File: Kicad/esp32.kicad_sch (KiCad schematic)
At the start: 29 parts, among them J3 TC2030-IDC, J4 Conn_01x04, J5 USB_C_Receptacle_USB2.0, SW1 GT-TC029B-H025-L1N, SW2 GT-TC029B-H025-L1N, U6 RT9080-33GJ5, U7 ESP32-S3-WROOM-1, Y1 32.768kHz

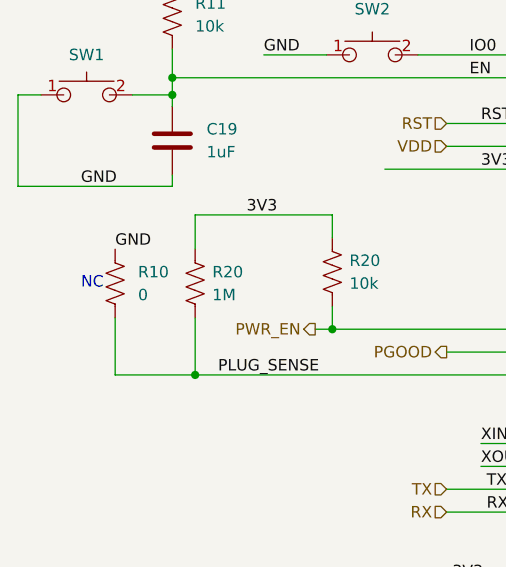
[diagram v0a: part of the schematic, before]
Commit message: Updating Bill Of Materials
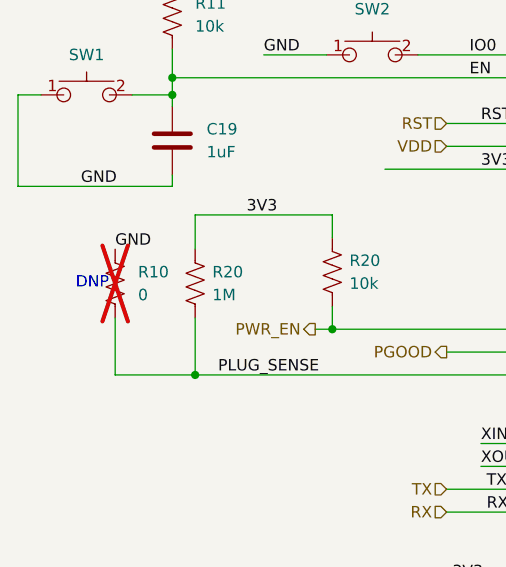
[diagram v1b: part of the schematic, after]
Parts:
- R10: now not fitted
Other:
- note added: "DNP"
- note removed: "NC"
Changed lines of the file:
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@@
 		)
 	)
-	(text "NC"
+	(text "DNP"
 		(exclude_from_sim no)
 		(at 26.67 102.87 0)
@@
 		(in_bom yes)
 		(on_board yes)
-		(dnp no)
+		(dnp yes)
 		(fields_autoplaced yes)
 		(property "Reference" "R10"

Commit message: V0.35 Release
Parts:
- removed R10: 0, Resistor_SMD:R_0402_1005Metric, symbol Device:R_US
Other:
- note removed: "DNP"
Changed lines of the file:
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@@
-	)
-	(junction
-		(at 38.1 113.03)
-		(diameter 0)
-		(color 0 0 0 0)
 	)
 	(junction
@@
 	(wire
 		(pts
-			(xy 29.21 113.03) (xy 29.21 106.68)
-		)
-		(stroke
-			(width 0)
-			(type default)
-		)
-	)
-	(wire
-		(pts
 			(xy 40.005 29.21) (xy 42.545 29.21)
 		)
@@
 		(pts
 			(xy 191.77 80.01) (xy 214.63 80.01)
-		)
-		(stroke
-			(width 0)
-			(type default)
-		)
-	)
-	(wire
-		(pts
-			(xy 38.1 113.03) (xy 29.21 113.03)
 		)
 		(stroke
@@
 		)
 	)
-	(text "DNP"
-		(exclude_from_sim no)
-		(at 26.67 102.87 0)
-		(effects
-			(font
-				(size 1.27 1.27)
-			)
-		)
-	)
 	(text "ESP32 3V3 LDO"
 		(exclude_from_sim no)
@@
 	(label "P_RX"
 		(at 51.435 170.815 0)
-		(fields_autoplaced yes)
-		(effects
-			(font
-				(size 1.27 1.27)
-			)
-			(justify left bottom)
-		)
-	)
-	(label "GND"
-		(at 29.21 99.06 0)
-		(fields_autoplaced yes)
 		(effects
 			(font
@@
 	(label "RST"
 		(at 69.85 85.09 0)
-		(fields_autoplaced yes)
 		(effects
 			(font
@@
 	(label "5V"
 		(at 204.47 53.975 0)
-		(fields_autoplaced yes)
 		(effects
 			(font
@@
 	(label "P_TX"
 		(at 51.435 168.275 0)
-		(fields_autoplaced yes)
 		(effects
 			(font
@@
 	(label "3V3"
 		(at 43.815 95.25 0)
-		(fields_autoplaced yes)
 		(effects
 			(font
@@
 	(label "EN"
 		(at 51.435 165.735 0)
-		(fields_autoplaced yes)
 		(effects
 			(font
@@
 	(label "GND"
 		(at 184.912 29.845 0)
-		(fields_autoplaced yes)
 		(effects
 			(font
@@
 	(label "GND"
 		(at 224.79 92.075 0)
-		(fields_autoplaced yes)
 		(effects
 			(font
@@
 	(label "XOUT32"
 		(at 150.495 29.845 0)
-		(fields_autoplaced yes)
 		(effects
 			(font
@@
 	(label "EN"
 		(at 68.58 80.01 0)
-		(fields_autoplaced yes)
 		(effects
 			(font
@@
 	(label "P_RX"
 		(at 195.58 90.17 0)
-		(fields_autoplaced yes)
 		(effects
 			(font
@@
 	(label "IO0"
 		(at 68.58 77.47 0)
-		(fields_autoplaced yes)
 		(effects
 			(font
@@
 	(label "GND"
 		(at 125.73 68.58 0)
-		(fields_autoplaced yes)
 		(effects
 			(font
@@
 	(label "3V3"
 		(at 66.675 135.89 0)
-		(fields_autoplaced yes)
 		(effects
 			(font
@@
 	(label "SDA"
 		(at 195.58 102.87 0)
-		(fields_autoplaced yes)
 		(effects
 			(font
@@
 	(label "GND"
 		(at 224.79 111.76 90)
-		(fields_autoplaced yes)
 		(effects
 			(font
@@
 	(label "GND"
 		(at 188.595 61.595 0)
-		(fields_autoplaced yes)
 		(effects
 			(font
@@
 	(label "XIN32"
 		(at 69.85 120.65 0)
-		(fields_autoplaced yes)
 		(effects
 			(font
@@
 	(label "TX"
 		(at 70.485 125.73 0)
-		(fields_autoplaced yes)
 		(effects
 			(font
@@
 	(label "GND"
 		(at 138.43 42.545 0)
-		(fields_autoplaced yes)
 		(effects
 			(font
@@
 	(label "3V3"
 		(at 76.835 165.735 0)
-		(fields_autoplaced yes)
 		(effects
 			(font
@@
 	(label "3V3"
 		(at 69.85 90.17 0)
-		(fields_autoplaced yes)
 		(effects
 			(font
@@
 	(label "IO0"
 		(at 76.835 170.815 0)
-		(fields_autoplaced yes)
 		(effects
 			(font
@@
 	(label "SCL"
 		(at 195.58 100.33 0)
-		(fields_autoplaced yes)
 		(effects
 			(font
@@
 	(label "XOUT32"
 		(at 69.85 123.19 0)
-		(fields_autoplaced yes)
 		(effects
 			(font
@@
 	(label "SCL"
 		(at 184.912 34.925 0)
-		(fields_autoplaced yes)
 		(effects
 			(font
@@
 	(label "XIN32"
 		(at 116.84 29.845 0)
-		(fields_autoplaced yes)
 		(effects
 			(font
@@
 	(label "GND"
 		(at 201.93 135.89 0)
-		(fields_autoplaced yes)
 		(effects
 			(font
@@
 	(label "GND"
 		(at 45.72 77.47 0)
-		(fields_autoplaced yes)
 		(effects
 			(font
@@
 	(label "SDA"
 		(at 184.912 37.465 0)
-		(fields_autoplaced yes)
 		(effects
 			(font
@@
 	(label "PLUG_SENSE"
 		(at 40.64 113.03 0)
-		(fields_autoplaced yes)
 		(effects
 			(font
@@
 	(label "3V3"
 		(at 125.73 55.88 0)
-		(fields_autoplaced yes)
 		(effects
 			(font
@@
 	(label "P_TX"
 		(at 195.58 87.63 0)
-		(fields_autoplaced yes)
 		(effects
 			(font
@@
 	(label "3V3"
 		(at 184.912 32.385 0)
-		(fields_autoplaced yes)
 		(effects
 			(font
@@
 	(label "GND"
 		(at 25.4 92.075 0)
-		(fields_autoplaced yes)
 		(effects
 			(font
@@
 	(label "5V"
 		(at 33.655 29.21 0)
-		(fields_autoplaced yes)
 		(effects
 			(font
@@
 	(label "GND"
 		(at 76.835 168.275 0)
-		(fields_autoplaced yes)
 		(effects
 			(font
@@
 	(label "GND"
 		(at 48.895 42.545 0)
-		(fields_autoplaced yes)
 		(effects
 			(font
@@
 	(label "3V3"
 		(at 35.56 66.675 0)
-		(fields_autoplaced yes)
 		(effects
 			(font
@@
 	(label "RX"
 		(at 70.485 128.27 0)
-		(fields_autoplaced yes)
 		(effects
 			(font
@@
 		(shape input)
 		(at 66.04 125.73 180)
-		(fields_autoplaced yes)
 		(effects
 			(font
@@
 		(shape input)
 		(at 66.04 128.27 180)
-		(fields_autoplaced yes)
 		(effects
 			(font
@@
 		(shape input)
 		(at 73.025 29.21 0)
-		(fields_autoplaced yes)
 		(effects
 			(font
@@
 		(shape input)
 		(at 200.025 100.33 0)
-		(fields_autoplaced yes)
 		(effects
 			(font
@@
 		(shape input)
 		(at 66.04 85.09 180)
-		(fields_autoplaced yes)
 		(effects
 			(font
@@
 		(shape input)
 		(at 200.025 102.87 0)
-		(fields_autoplaced yes)
 		(effects
 			(font
@@
 		(shape output)
 		(at 66.04 110.49 180)
-		(fields_autoplaced yes)
 		(effects
 			(font
@@
 		(shape output)
 		(at 51.435 107.95 180)
-		(fields_autoplaced yes)
 		(effects
 			(font
@@
 		(shape input)
 		(at 23.495 29.21 180)
-		(fields_autoplaced yes)
 		(effects
 			(font
@@
 		(shape input)
 		(at 66.04 87.63 180)
-		(fields_autoplaced yes)
 		(effects
 			(font
@@
 					(unit 1)
 				)
-			)
-		)
-	)
-	(symbol
-		(lib_id "Device:R_US")
-		(at 29.21 102.87 180)
-		(unit 1)
-		(exclude_from_sim no)
-		(in_bom yes)
-		(on_board yes)
-		(dnp yes)
-		(fields_autoplaced yes)
-		(property "Reference" "R10"
-			(at 31.75 101.5999 0)
-			(effects
-				(font
-					(size 1.27 1.27)
-				)
-				(justify right)
-			)
-		)
-		(property "Value" "0"
-			(at 31.75 104.1399 0)
-			(effects
-				(font
-					(size 1.27 1.27)
-				)
-				(justify right)
-			)
-		)
-		(property "Footprint" "Resistor_SMD:R_0402_1005Metric"
-			(at 28.194 102.616 90)
-			(effects
-				(font
-					(size 1.27 1.27)
-				)
-				(hide yes)
-			)
-		)
-		(property "Datasheet" "~"
-			(at 29.21 102.87 0)
-			(effects
-				(font
-					(size 1.27 1.27)
-				)
-				(hide yes)
-			)
-		)
-		(property "Description" ""
-			(at 29.21 102.87 0)
-			(effects
-				(font
-					(size 1.27 1.27)
-				)
-				(hide yes)
-			)
-		)
-		(property "DK" "311-1.00MLRCT-ND"
-			(at 29.21 102.87 0)
-			(effects
-				(font
-					(size 1.27 1.27)
-				)
-				(hide yes)
-			)
-		)
-		(property "PARTNO" "RC0402FR-071ML"
-			(at 29.21 102.87 0)
-			(effects
-				(font
-					(size 1.27 1.27)
-				)
-				(hide yes)
-			)
-		)
-		(pin "1"
-		)
-		(pin "2"
-		)
-		(instances
-			(project "bitaxeUltra"
-				(path "/e63e39d7-6ac0-4ffd-8aa3-1841a4541b55/ca857324-2ec8-447e-bd58-90d0c2e6b6d7"
-					(reference "R10")
-					(unit 1)
-				)
